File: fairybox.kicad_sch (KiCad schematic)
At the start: 65 parts, among them J1 REED, Q1 SI2302, Q10 C114, Q2 C3200, Q3 C114, Q4 C114, Q5 C3200, Q6 C114, Q7 C114, Q8 C114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

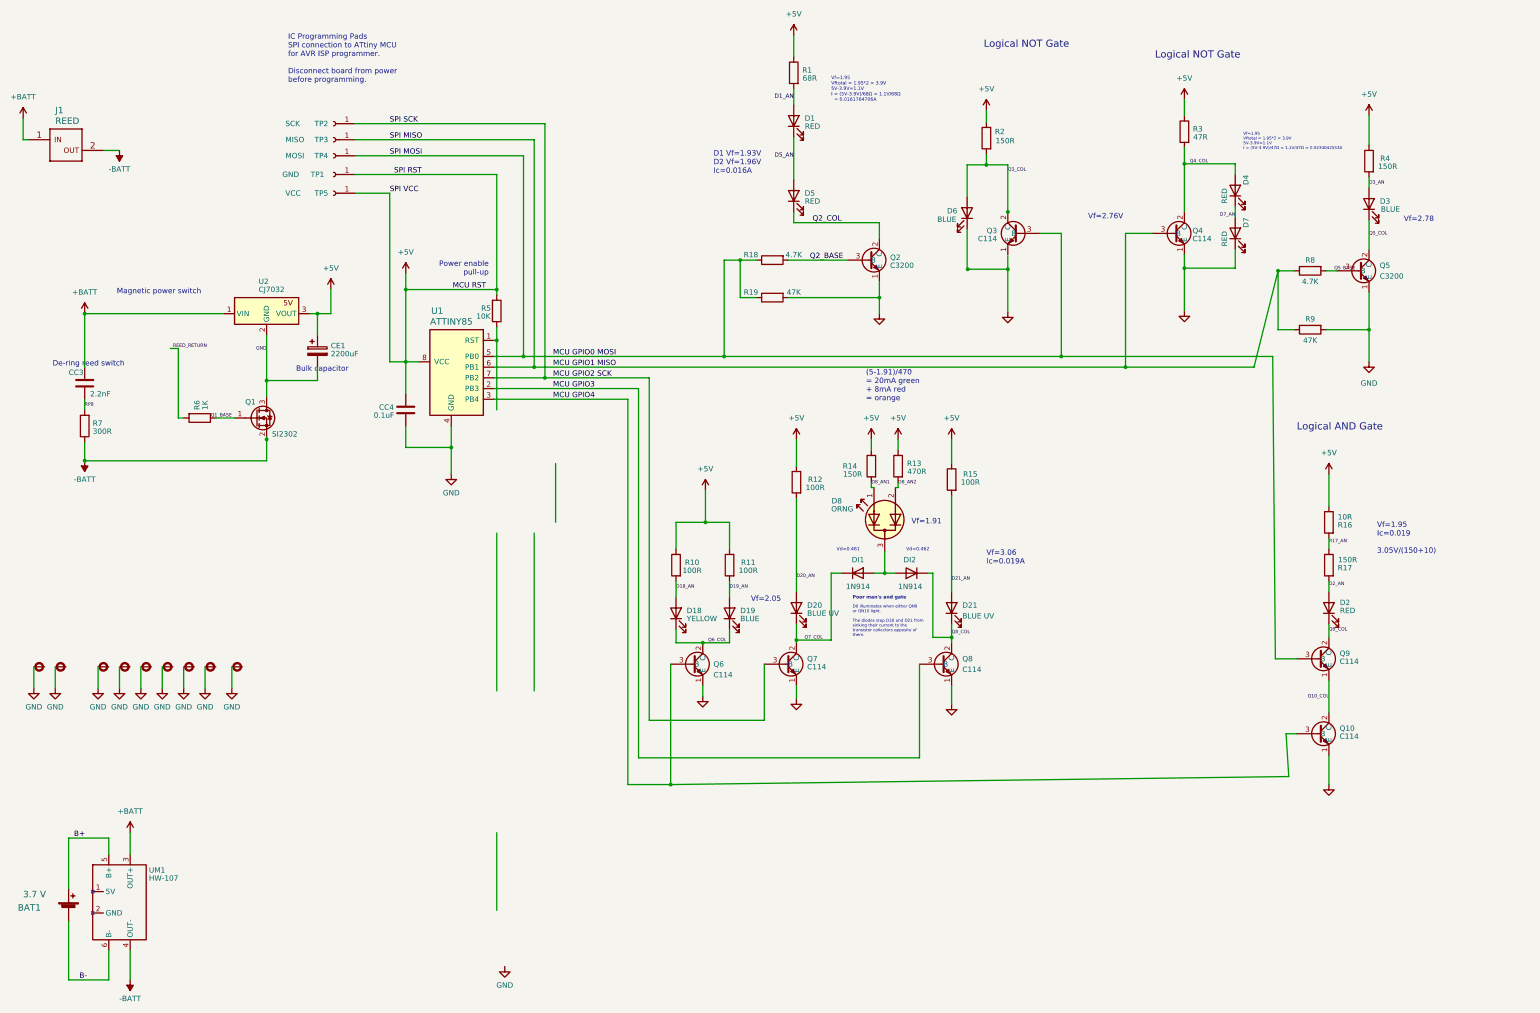
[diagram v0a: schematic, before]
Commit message: GPIO Assignment Changes
In order to enable more efficient signal trace routing transistor base pins were reassigned to different MCU signal pins. The new order no longer has signal traces crossing paths to get to their destination. In other words, it's eliminated the need for any vias to the ground plane. 

This routing is much simpler and improves the chances of a successful (functioning) PCB. 
- Easier to manufacture. Not pushing JLCPCB's manufacturing capabilities is a good thing.
- Likely less unintended EMI radiation. 
- Less opportunities for signal crosstalk.
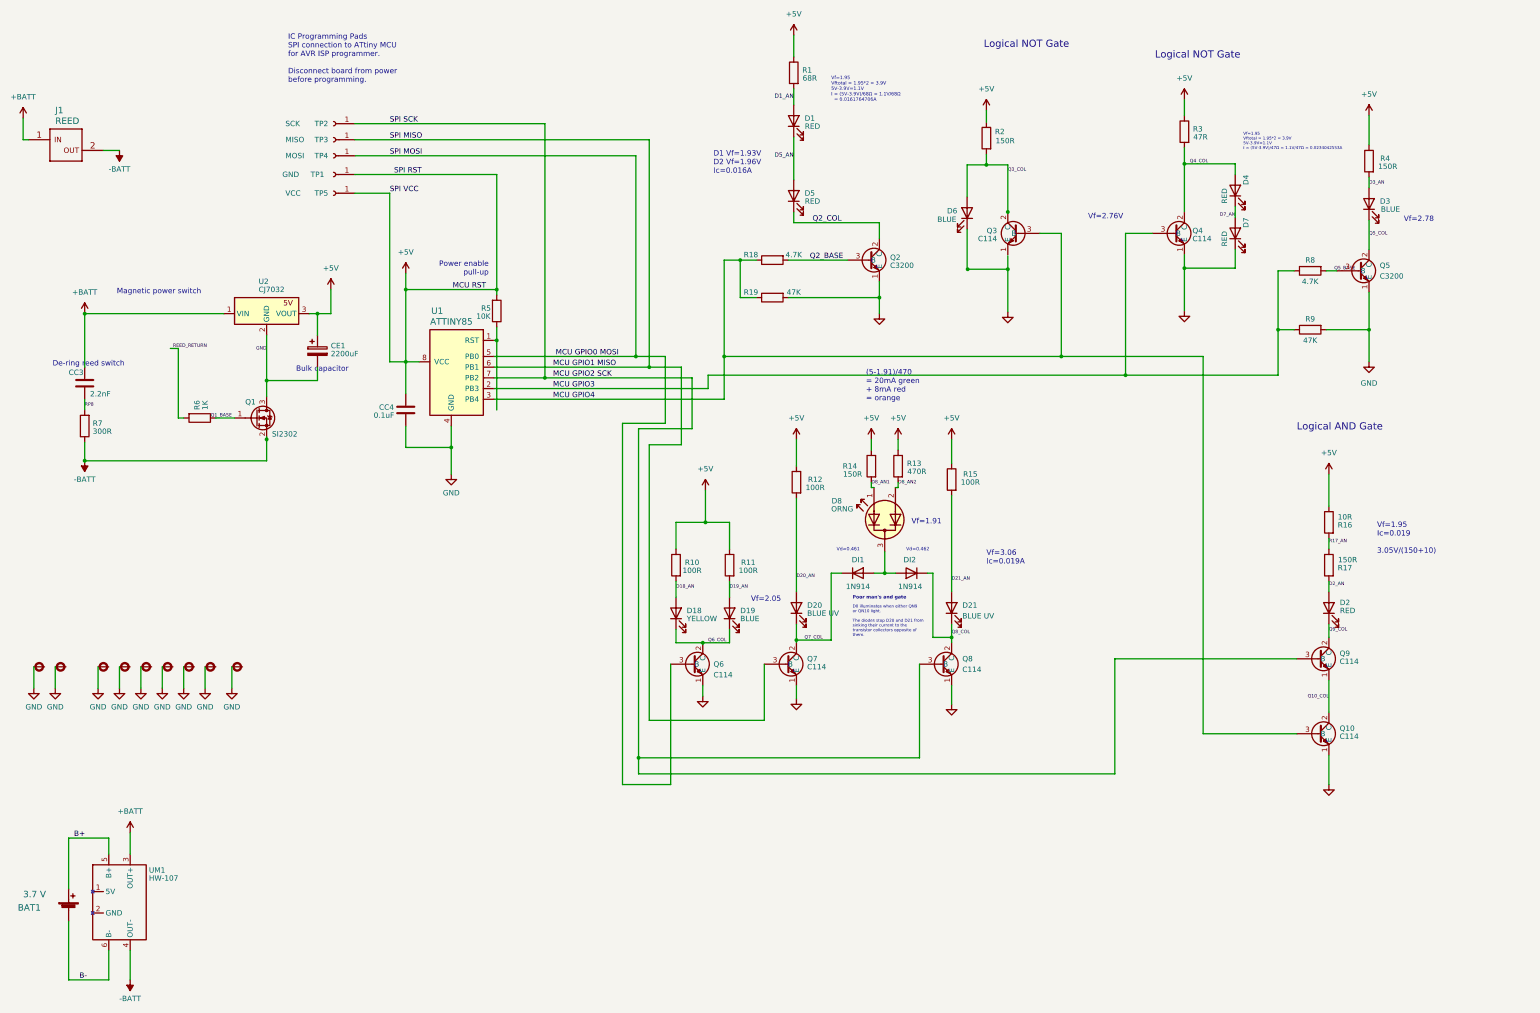
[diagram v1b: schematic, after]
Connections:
- net MCU GPIO0 MOSI: now also Q6.3 (B); no longer Q3.3 (B), Q9.3 (B), R18.1, R19.1
- net MCU GPIO1 MISO: now also Q7.3 (B); no longer Q4.3 (B), R8.1, R9.1
- net MCU GPIO2 SCK: now also Q8.3 (B), Q9.3 (B); no longer Q7.3 (B)
- net MCU GPIO3: now also Q4.3 (B), R8.1, R9.1; no longer Q8.3 (B)
- net MCU GPIO4: now also Q3.3 (B), R18.1, R19.1; no longer Q6.3 (B)

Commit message: Update fairybox.kicad_sch
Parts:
- removed R16: 10R, Resistor_THT:R_Axial_DIN0204_L3.6mm_D1.6mm_P5.08mm_Horizontal, symbol Device:R
- added TP10, TP11, TP12, TP6, TP7, TP8, TP9: TestPoint_Small, TestPoint:TestPoint_Pad_D1.0mm, symbol Connector:TestPoint_Small
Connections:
- net R17_AN is gone; now on net +5V: R17.1
- net +5V: no longer TP1.1 (Pin_1)
- net -BATT: no longer J1.2
- net GND: now also Q3.1 (E)
- net Q10_COL: now also TP12.1
- net Q2_COL: now also TP8.1
- net Q3_COL: now also TP7.1
- net Q4_COL: now also TP6.1
- net Q5_COL: now also TP9.1
- net Q8_COL: now also TP10.1
- net Q9_COL: now also TP11.1
- net REED_RETURN: now also J1.2
- net SPI RST: now reaches R5.1, U1.1 (RST)
- net SPI RST: now also TP1.1 (Pin_1)
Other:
- note added: "2.68V * .0178A = 47mW"
- note added: "Power"
- note added: "Rc = 50Ω"
- note added: "Vf=2.36 @ 17mA (5V-2.36V) / 150Ω 2.68V / .0178A"
- note added: "Voltage / Current / Resistance"
- note removed: "Vf=1.95 Ic=0.019 3.05V/(150+10)"
